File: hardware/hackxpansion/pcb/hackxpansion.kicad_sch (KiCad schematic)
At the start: 0 parts

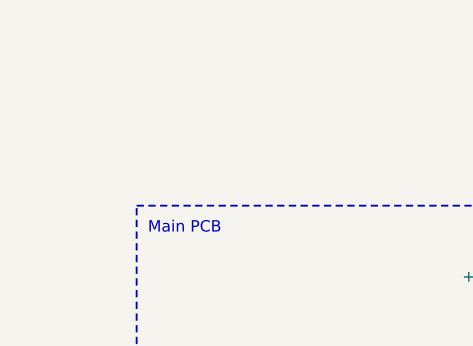
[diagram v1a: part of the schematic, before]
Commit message: added silkscreen
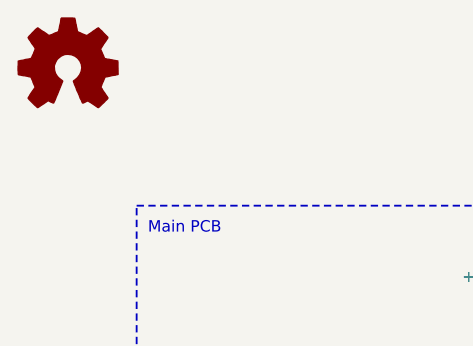
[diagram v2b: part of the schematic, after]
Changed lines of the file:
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@@
+	)
+	(symbol
+		(lib_id "Graphic:Logo_Open_Hardware_Small")
+		(at 19.05 19.05 0)
+		(unit 1)
+		(body_style 1)
+		(exclude_from_sim no)
+		(in_bom no)
+		(on_board no)
+		(in_pos_files yes)
+		(dnp no)
+		(fields_autoplaced yes)
+		(property "Reference" "#SYM3"
+			(at 19.05 12.065 0)
+			(hide yes)
+			(show_name no)
+			(do_not_autoplace no)
+			(effects
+				(font
+					(size 1.27 1.27)
+				)
+			)
+		)
+		(property "Value" "Logo_Open_Hardware_Small"
+			(at 19.05 24.765 0)
+			(hide yes)
+			(show_name no)
+			(do_not_autoplace no)
+			(effects
+				(font
+					(size 1.27 1.27)
+				)
+			)
+		)
+		(property "Footprint" ""
+			(at 19.05 19.05 0)
+			(hide yes)
+			(show_name no)
+			(do_not_autoplace no)
+			(effects
+				(font
+					(size 1.27 1.27)
+				)
+			)
+		)
+		(property "Datasheet" ""
+			(at 19.05 19.05 0)
+			(hide yes)
+			(show_name no)
+			(do_not_autoplace no)
+			(effects
+				(font
+					(size 1.27 1.27)
+				)
+			)
+		)
+		(property "Description" "Open Hardware logo, small"
+			(at 19.05 19.05 0)
+			(hide yes)
+			(show_name no)
+			(do_not_autoplace no)
+			(effects
+				(font
+					(size 1.27 1.27)
+				)
+			)
+		)
+		(property "Sim.Enable" "0"
+			(at 19.05 19.05 0)
+			(hide yes)
+			(show_name no)
+			(do_not_autoplace no)
+			(effects
+				(font
+					(size 1.27 1.27)
+				)
+			)
+		)
+		(instances
+			(project "hackxpansion"
+				(path "/aaf5804d-3f78-442b-969e-39faa388db94"
+					(reference "#SYM3")
+					(unit 1)
+				)
+			)
+		)
 	)
 	(symbol
